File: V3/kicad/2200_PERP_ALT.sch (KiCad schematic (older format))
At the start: 6 parts, among them J2200 Conn_01x08_Male, J2201 Conn_01x08_Male, U2200 PIO-LQFP-44

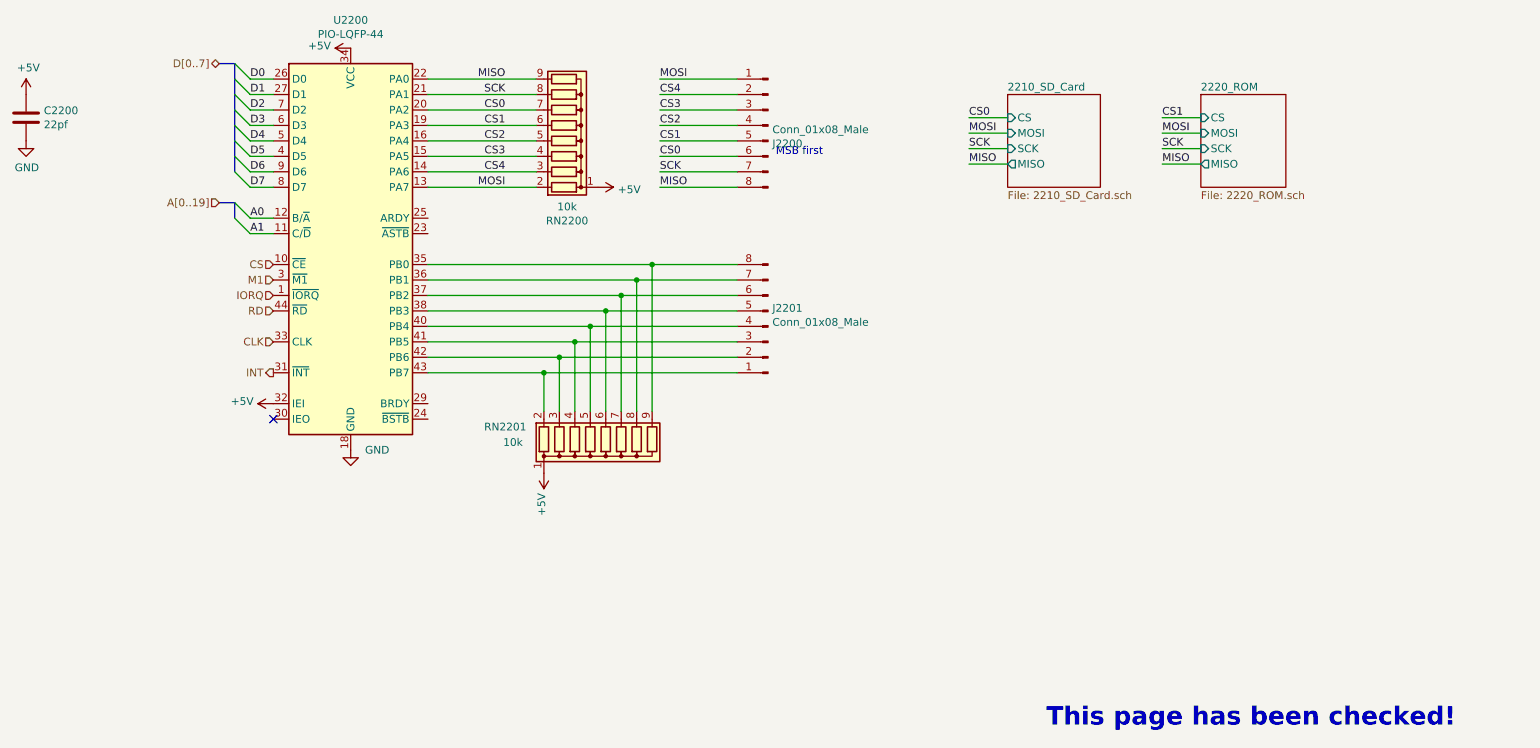
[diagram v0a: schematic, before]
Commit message: 3 1 1 m memory (#15)
* moved EEPROM files to /old

* Reworking 3.0 board

* changed footprint on RAM chip

* cleared out old memory traces

* started on rerouting

* on to autoroute

* little more cleanup

* more cleanup

* ill let the autoroute do the rest

* reroute complete

* made PQFP leads fatter

* Updated GAL logic

* Design Rule Check

* Minor pcb touch up

* gerber files

* just totally redid the whole thing

* More rearranging

* added a few caps

* Routed ROM and RAM together

* more routing

* more routes

* A lot of disorganized changes

* 3.1 CSIO SPI Bus (#9)

* Updated SPI to use CPU signals

8 bit register chip controls CS lines

* Renamed and added caps to SD page

* Cleanup

* 3.1 Resistor Replacement (#10)

* First two R arrays

* Added one more r array

* added cap for SPI FF

* Extended cpu pads (#12)

* 3.1 fix sheet hierarchy (#13)

* Fixed Schematic Heirarchy issue

* some footprints re-added to board

* Add footprints added

* Minor changes

* 3.1 redraw cpu courtyard (#14)

* moved all crtyd lines to same place in file

* Duplicate lines were causing issues

* Added pin header for SPI lines

* routed last of non-bus lines

* attempted to route memory lines

* Added new symbol and footprint

* CTS0 no longer drives an LED

* Final cleanup before memory routing

* got CTS0 and RTS mixed up

* Removed extra led from board

* Updated signature

* small changes
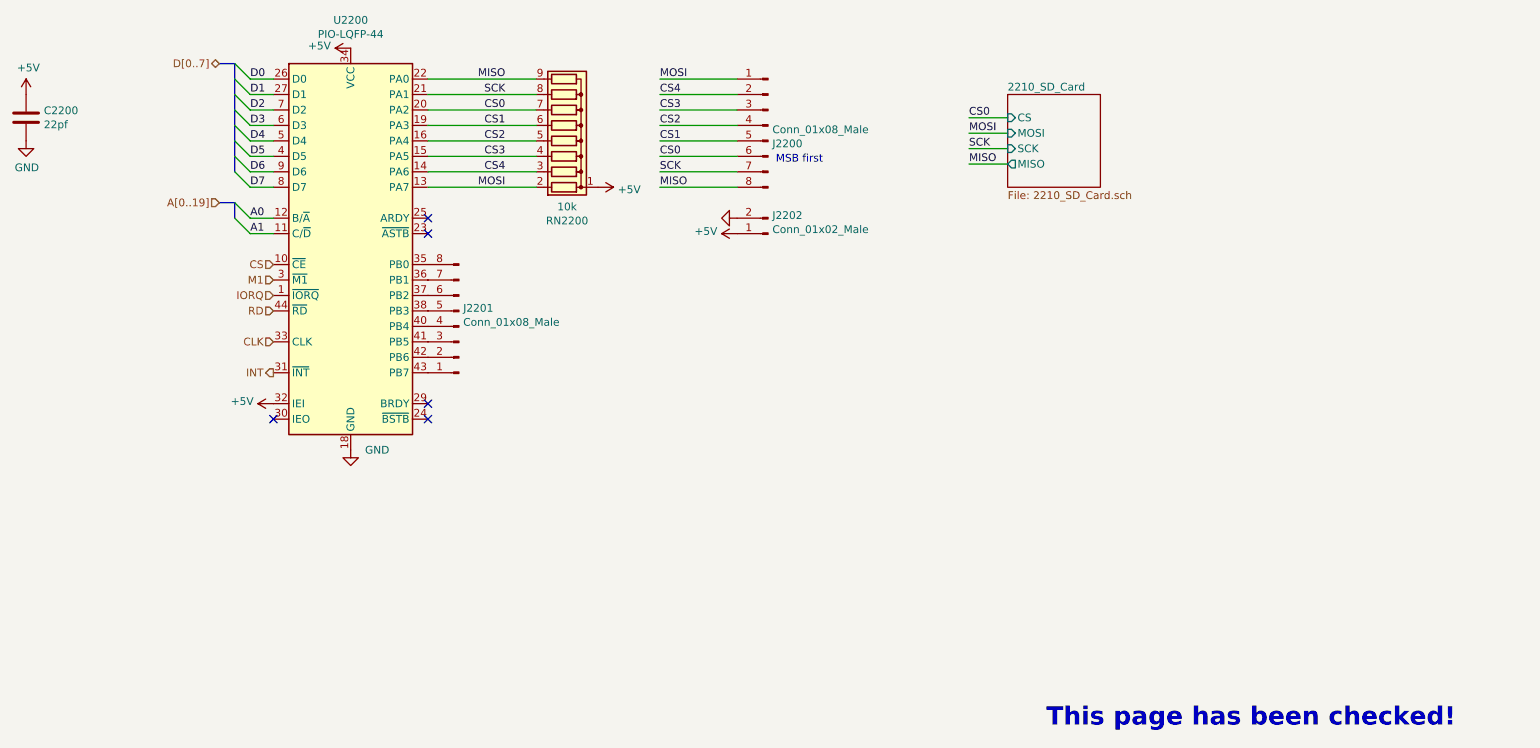
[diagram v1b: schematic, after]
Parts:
- removed RN2201: 10k, Resistor_THT:R_Array_SIP9, symbol Device:R_Network08
- added J2202: Conn_01x02_Male, Connector_PinHeader_2.54mm:PinHeader_1x02_P2.54mm_Vertical, symbol Connector:Conn_01x02_Male
- C2200: footprint Capacitor_THT:C_Rect_L4.0mm_W2.5mm_P2.50mm -> Capacitor_SMD:C_1206_3216Metric
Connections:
- net +5V: now also J2202.1 (Pin_1)
- net GND: now also J2202.2 (Pin_2)
- no-connect marks 1 -> 5
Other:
- moved on the sheet: J2201
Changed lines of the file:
@@
 $Descr A4 11693 8268
 encoding utf-8
-Sheet 4 9
+Sheet 4 8
 Title ""
 Date ""
@@
 	1    0    0    -1
 $EndComp
-Text Notes 6100 3250 0    50   ~ 0
+Text Notes 6100 3300 0    50   ~ 0
 MSB first
 Text HLabel 2850 4650 0    50   Output ~ 0
@@
 	0    1    1    0
 $EndComp
-$Comp
-L Device:R_Network08 RN2201
-U 1 1 62184408
-P 5000 5100
-F 0 "RN2201" H 4350 5000 50  0000 C CNN
-F 1 "10k" H 4400 5100 50  0000 C CNN
-F 2 "Resistor_THT:R_Array_SIP9" V 5475 5100 50  0001 C CNN
-F 3 "http://www.vishay.com/docs/31509/csc.pdf" H 5000 5100 50  0001 C CNN
-	1    5000 5100
-	1    0    0    1
-$EndComp
-$Comp
-L power:+5V #PWR0129
-U 1 1 62184416
-P 4600 5300
-F 0 "#PWR0129" H 4600 5150 50  0001 C CNN
-F 1 "+5V" V 4615 5428 50  0000 L CNN
-F 2 "" H 4600 5300 50  0001 C CNN
-F 3 "" H 4600 5300 50  0001 C CNN
-	1    4600 5300
-	-1   0    0    1
-$EndComp
 $Sheet
 S 7600 2850 600  600
@@
 Wire Wire Line
 	7350 3000 7600 3000
-$Sheet
-S 8850 2850 550  600
-U 62602013
-F0 "2220_ROM" 50
-F1 "2220_ROM.sch" 50
-F2 "CS" I L 8850 3000 50
-F3 "MOSI" I L 8850 3100 50
-F4 "MISO" O L 8850 3300 50
-F5 "SCK" I L 8850 3200 50
-$EndSheet
 Text Notes 7850 6950 0    118  ~ 24
 This page has been checked!
-Wire Wire Line
-	8850 3100 8600 3100
-Wire Wire Line
-	8850 3200 8600 3200
-Text Label 8600 3100 0    50   ~ 0
-MOSI
-Text Label 8600 3200 0    50   ~ 0
-SCK
-Text Label 8600 3300 0    50   ~ 0
-MISO
-Wire Wire Line
-	8850 3300 8600 3300
-Text Label 8600 3000 0    50   ~ 0
-CS1
-Wire Wire Line
-	8600 3000 8850 3000
 $Comp
 L Connector:Conn_01x08_Male J2201
 U 1 1 6261A38A
-P 6050 4350
-F 0 "J2201" H 6022 4232 50  0000 R CNN
-F 1 "Conn_01x08_Male" H 6022 4323 50  0000 R CNN
-F 2 "Connector_PinHeader_2.54mm:PinHeader_1x08_P2.54mm_Vertical" H 6050 4350 50  0001 C CNN
-F 3 "~" H 6050 4350 50  0001 C CNN
-	1    6050 4350
+P 4050 4350
+F 0 "J2201" H 4022 4232 50  0000 R CNN
+F 1 "Conn_01x08_Male" H 4022 4323 50  0000 R CNN
+F 2 "Connector_PinHeader_2.54mm:PinHeader_1x08_P2.54mm_Vertical" H 4050 4350 50  0001 C CNN
+F 3 "~" H 4050 4350 50  0001 C CNN
+	1    4050 4350
 	-1   0    0    1
 $EndComp
-Wire Wire Line
-	3850 4650 4600 4650
-Wire Wire Line
-	4600 4900 4600 4650
-Connection ~ 4600 4650
-Wire Wire Line
-	4600 4650 5850 4650
-Wire Wire Line
-	3850 4550 4700 4550
-Wire Wire Line
-	3850 4450 4800 4450
-Wire Wire Line
-	4700 4900 4700 4550
-Connection ~ 4700 4550
-Wire Wire Line
-	4700 4550 5850 4550
-Wire Wire Line
-	4800 4900 4800 4450
-Connection ~ 4800 4450
-Wire Wire Line
-	4800 4450 5850 4450
-Wire Wire Line
-	3850 4350 4900 4350
-Wire Wire Line
-	3850 4250 5000 4250
-Wire Wire Line
-	3850 4150 5100 4150
-Wire Wire Line
-	3850 4050 5200 4050
-Wire Wire Line
-	3850 3950 5300 3950
-Wire Wire Line
-	4900 4900 4900 4350
-Connection ~ 4900 4350
-Wire Wire Line
-	5100 4900 5100 4150
-Connection ~ 5100 4150
-Wire Wire Line
-	5100 4150 5850 4150
-Connection ~ 5000 4250
-Wire Wire Line
-	5000 4250 5850 4250
-Wire Wire Line
-	5000 4250 5000 4900
-Wire Wire Line
-	4900 4350 5850 4350
-Wire Wire Line
-	5200 4900 5200 4050
-Connection ~ 5200 4050
-Wire Wire Line
-	5200 4050 5850 4050
-Wire Wire Line
-	5300 4900 5300 3950
-Connection ~ 5300 3950
-Wire Wire Line
-	5300 3950 5850 3950
 $Comp
 L Device:C C?
@@
 F 0 "C2200" H 1365 3046 50  0000 L CNN
 F 1 "22pf" H 1365 2955 50  0000 L CNN
-F 2 "Capacitor_THT:C_Rect_L4.0mm_W2.5mm_P2.50mm" H 1288 2850 50  0001 C CNN
+F 2 "Capacitor_SMD:C_1206_3216Metric" H 1288 2850 50  0001 C CNN
 F 3 "~" H 1250 3000 50  0001 C CNN
 	1    1250 3000
@@
 	1    0    0    -1
 $EndComp
+NoConn ~ 3850 4850
+NoConn ~ 3850 4950
+NoConn ~ 3850 3650
+NoConn ~ 3850 3750
+$Comp
+L Connector:Conn_01x02_Male J2202
+U 1 1 62EBE199
+P 6050 3750
+F 0 "J2202" H 6022 3632 50  0000 R CNN
+F 1 "Conn_01x02_Male" H 6022 3723 50  0000 R CNN
+F 2 "Connector_PinHeader_2.54mm:PinHeader_1x02_P2.54mm_Vertical" H 6050 3750 50  0001 C CNN
+F 3 "~" H 6050 3750 50  0001 C CNN
+	1    6050 3750
+	-1   0    0    1
+$EndComp
+$Comp
+L power:+5V #PWR0159
+U 1 1 62EBEF84
+P 5850 3750
+F 0 "#PWR0159" H 5850 3600 50  0001 C CNN
+F 1 "+5V" V 5865 3878 50  0000 L CNN
+F 2 "" H 5850 3750 50  0001 C CNN
+F 3 "" H 5850 3750 50  0001 C CNN
+	1    5850 3750
+	0    -1   -1   0
+$EndComp
+$Comp
+L power:GND #PWR0163
+U 1 1 62EBFB90
+P 5850 3650
+F 0 "#PWR0163" H 5850 3400 50  0001 C CNN
+F 1 "GND" H 5850 3350 50  0001 R CNN
+F 2 "" H 5850 3650 50  0001 C CNN
+F 3 "" H 5850 3650 50  0001 C CNN
+	1    5850 3650
+	0    1    1    0
+$EndComp
 Wire Bus Line
